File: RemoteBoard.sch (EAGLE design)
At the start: 10 parts, among them U1 SPG30, U2 TXS0102DCU, U3 MIC53651.8SC70, U4 BME280

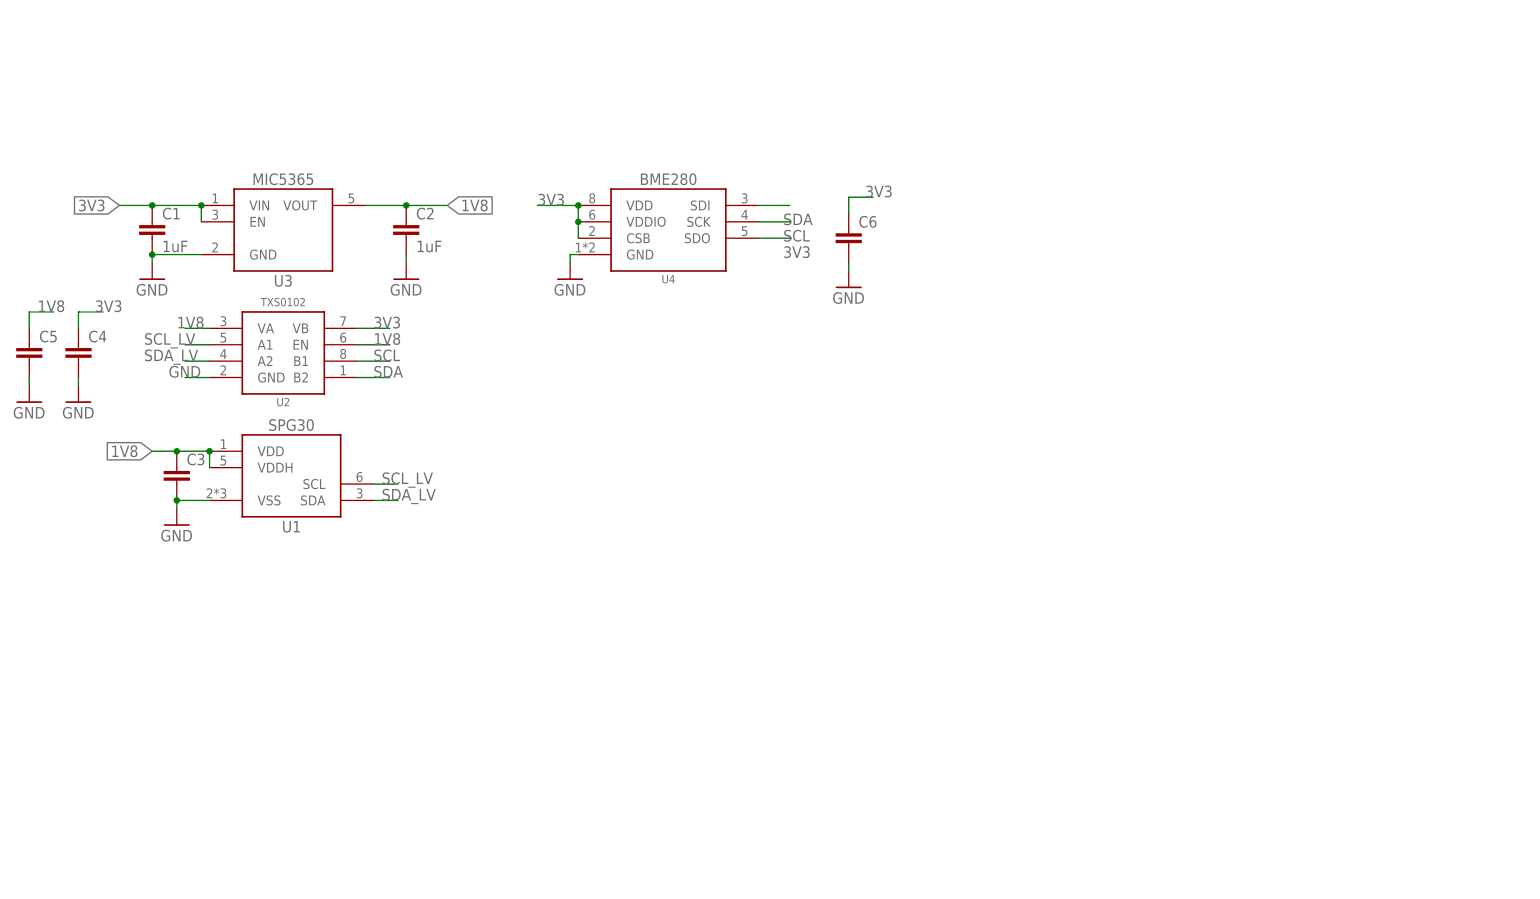
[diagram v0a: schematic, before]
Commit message: Continued schematic capture for remote board, layout begin
Schematic for remote board complete except for TCS3400, significant layout progress
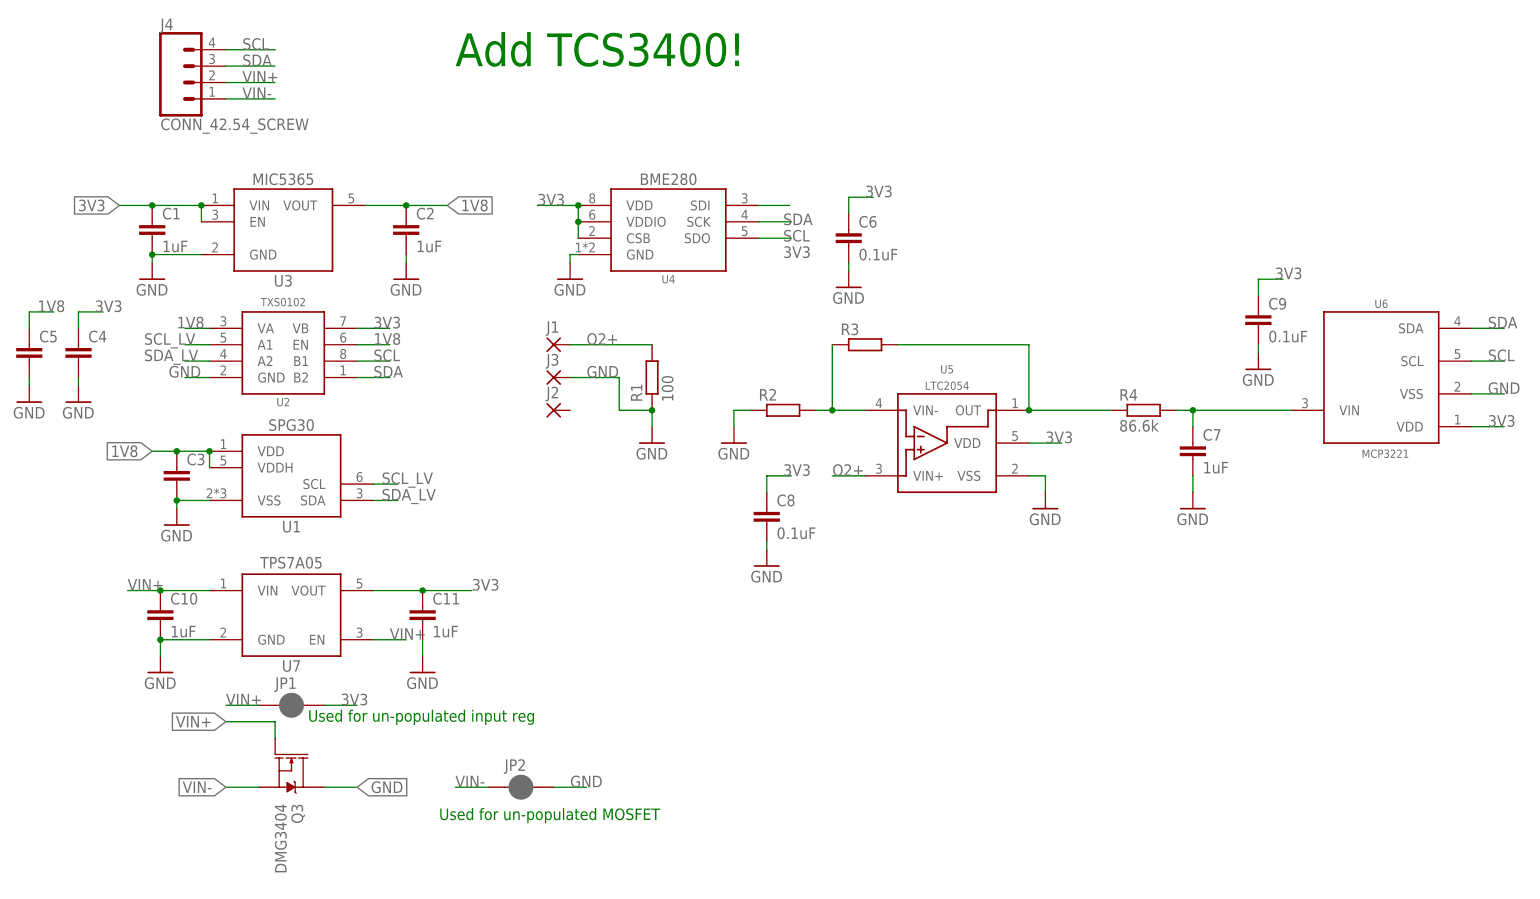
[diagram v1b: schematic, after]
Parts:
- added C10, C11: 1uF, bschulz_passives:C-EUC0805
- added C7: 1uF, bschulz:C-EUC0805
- added C8, C9: 0.1uF, bschulz:C-EUC0805
- added J1, J2, J3: SOCKETS9111, bschulz:SOCKETS9111
- added J4: CONN_42.54_SCREW, bschulz:CONN_42.54_SCREW
- added JP1, JP2: JUMPER-SMT_2_NC_PASTE_SILK, SparkFun-Jumpers:JUMPER-SMT_2_NC_PASTE_SILK
- added Q3: DMG3404, bschulz:MOSFET-NCH-DMG3404L
- added R1: 100, bschulz:R-EU_R0805
- added R2, R3: (no value), bschulz:R-EU_R0805
- added R4: 86.6k, bschulz:R-EU_R0805
- added U5: LTC2054, bschulz:LTC2054
- added U6: MCP3221, bschulz:MCP3221
- added U7: TPS7A0533DBV, bschulz:TPS7A0533DBV
- C1, C2: device bschulz_passives:C-EU1UFC0603 -> bschulz:C-EUC0805
- C3, C4, C5: device bschulz_passives:C-EU0.1UFC0603 -> bschulz:C-EUC0805
- C6: value (none) -> 0.1uF; device bschulz_passives:C-EU0.1UFC0603 -> bschulz:C-EUC0805
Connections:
- new net N$1: R2.2, R3.1, U5.VIN-
- new net N$2: R3.2, R4.1, U5.OUT
- new net N$3: C7.1, R4.2, U6.VIN
- new net O2+: J1.P, R1.2, U5.VIN+
- new net VIN+: C10.1, J4.2, JP1.1, Q3.G, U7.EN, U7.VIN
- new net VIN-: J4.1, JP2.1, Q3.S
- net 3V3: now also C11.1, C8.1, C9.1, JP1.2, U5.VDD, U6.VDD, U7.VOUT
- net GND: now also C10.2, C11.2, C7.2, C8.2, C9.2, J3.P, JP2.2, Q3.D, R1.1, R2.1, U5.VSS, U6.VSS, U7.GND
- net SCL: now also J4.4, U6.SCL
- net SDA: now also J4.3, U6.SDA
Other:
- note added: "Add TCS3400!"
- note added: "Used for un-populated MOSFET"
- note added: "Used for un-populated input reg"

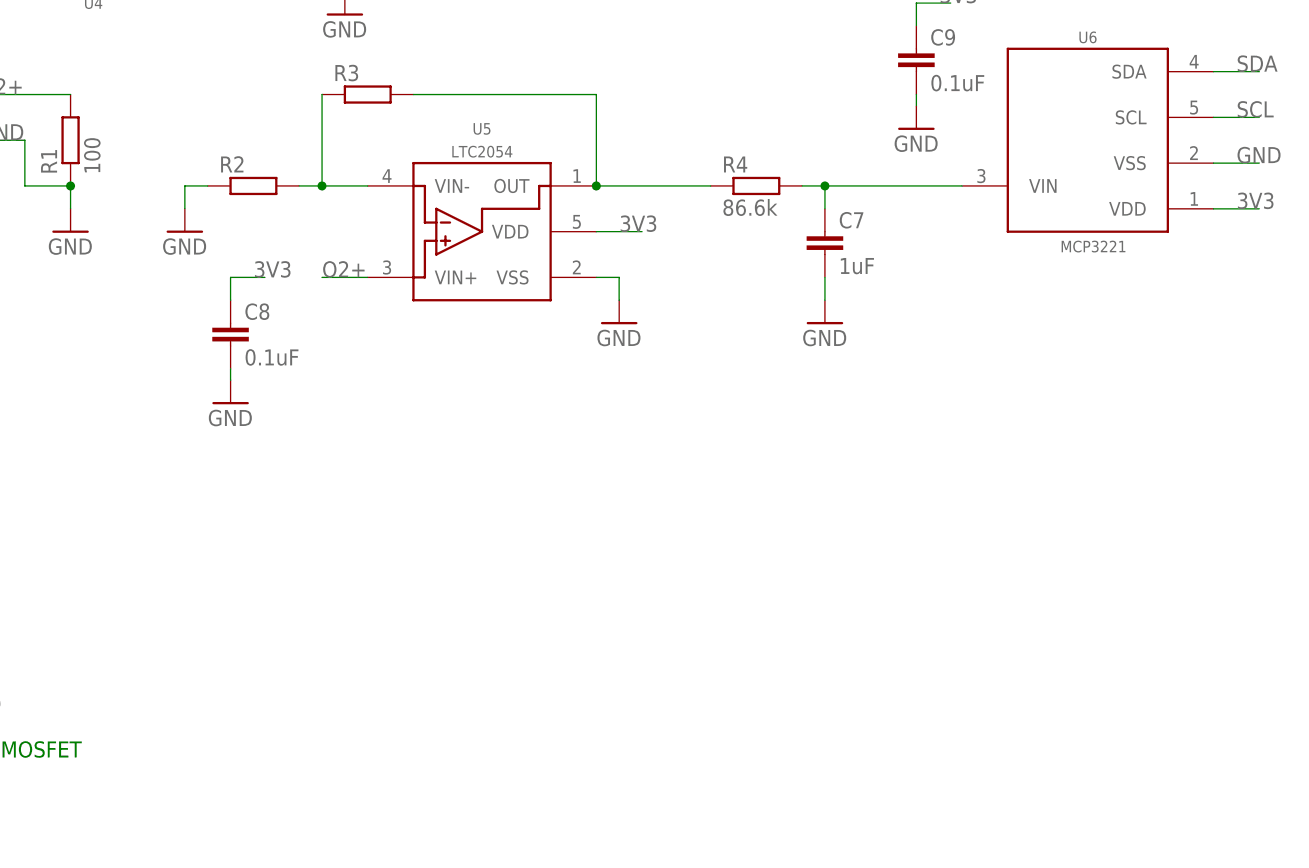
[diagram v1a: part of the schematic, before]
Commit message: Minor updates to Primary and Remote
Cleaned up/added silkscreen, added test points to both boards
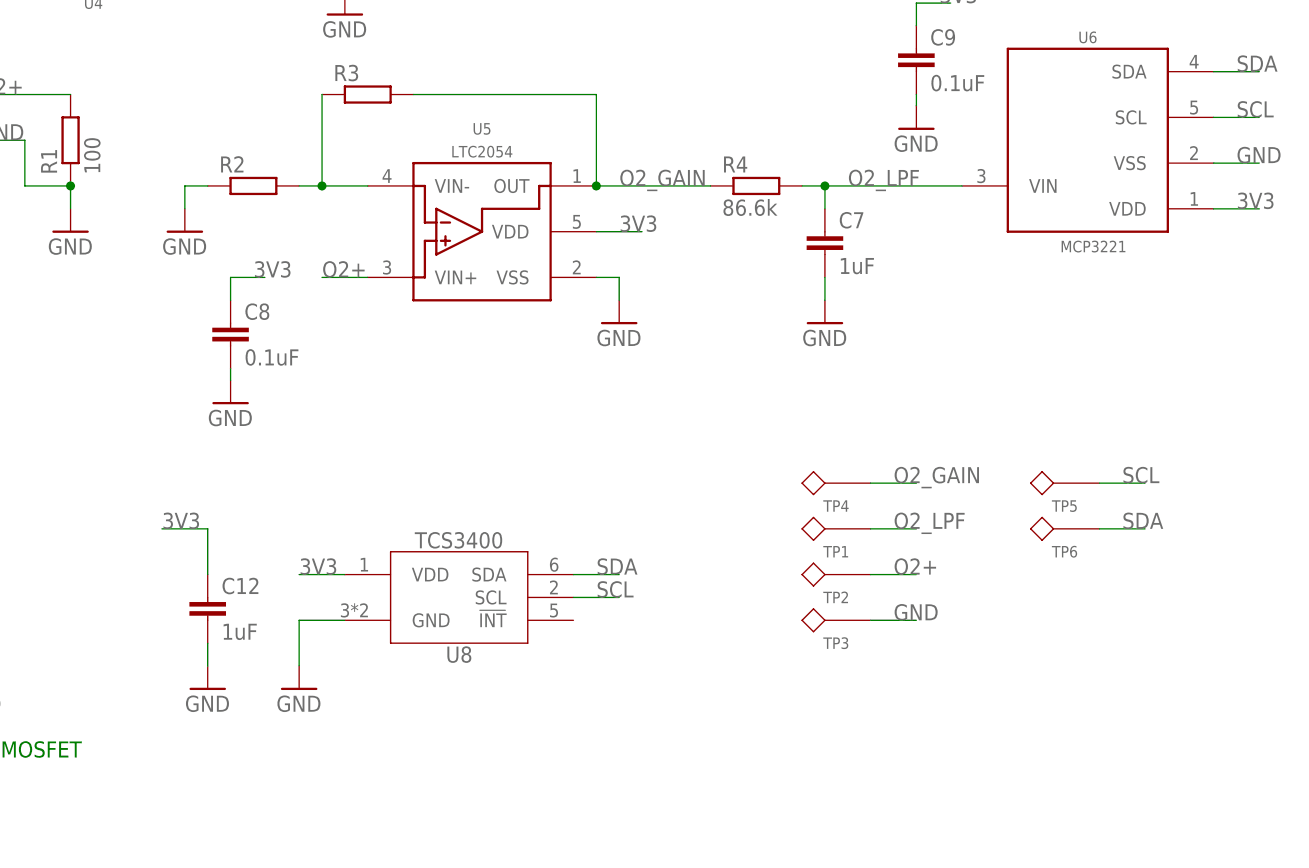
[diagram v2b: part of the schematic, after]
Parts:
- added C12: 1uF, bschulz_passives:C-EUC0805
- added TP1, TP2, TP3, TP4, TP5, TP6: TESTPOINTRCU, bschulz:TESTPOINTRCU
- added U8: TCS3400, bschulz:TCS3400
- C9: device bschulz:C-EUC0805 -> bschulz_passives:C-EUC0805
- J1, J2, J3: value SOCKETS9111 -> SOCKETS9111_SLOT; device bschulz:SOCKETS9111 -> bschulz:SOCKETS9111_SLOT
- R1, R2, R3, R4: device bschulz:R-EU_R0805 -> bschulz_passives:R-EU_R0805
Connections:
- removed net N$2: R3.2, R4.1, U5.OUT
- removed net N$3: C7.1, R4.2, U6.VIN
- new net O2_GAIN: R3.2, R4.1, TP4.P$1, U5.OUT
- new net O2_LPF: C7.1, R4.2, TP1.P$1, U6.VIN
- net 3V3: now also C12.1, U8.VDD
- net GND: now also C12.2, TP3.P$1, U8.GND
- net O2+: now also TP2.P$1
- net SCL: now also TP5.P$1, U8.SCL
- net SDA: now also TP6.P$1, U8.SDA
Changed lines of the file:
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@@
 <part name="C6" library="bschulz" deviceset="C-EU" device="C0805" value="0.1uF"/>
 <part name="GND7" library="supply1" library_urn="urn:adsk.eagle:library:371" deviceset="GND" device=""/>
-<part name="J1" library="bschulz" deviceset="SOCKET" device="S9111"/>
-<part name="J2" library="bschulz" deviceset="SOCKET" device="S9111"/>
-<part name="J3" library="bschulz" deviceset="SOCKET" device="S9111"/>
+<part name="J1" library="bschulz" deviceset="SOCKET" device="S9111_SLOT" value="SOCKETS9111_SLOT"/>
+<part name="J2" library="bschulz" deviceset="SOCKET" device="S9111_SLOT" value="SOCKETS9111_SLOT"/>
+<part name="J3" library="bschulz" deviceset="SOCKET" device="S9111_SLOT" value="SOCKETS9111_SLOT"/>
 <part name="U5" library="bschulz" deviceset="LTC2054" device=""/>
-<part name="R1" library="bschulz" deviceset="R-EU_" device="R0805" value="100"/>
+<part name="R1" library="bschulz_passives" deviceset="R-EU_" device="R0805" value="100"/>
 <part name="GND8" library="supply1" library_urn="urn:adsk.eagle:library:371" deviceset="GND" device=""/>
-<part name="R2" library="bschulz" deviceset="R-EU_" device="R0805"/>
-<part name="R3" library="bschulz" deviceset="R-EU_" device="R0805"/>
+<part name="R2" library="bschulz_passives" deviceset="R-EU_" device="R0805"/>
+<part name="R3" library="bschulz_passives" deviceset="R-EU_" device="R0805"/>
 <part name="GND9" library="supply1" library_urn="urn:adsk.eagle:library:371" deviceset="GND" device=""/>
 <part name="GND10" library="supply1" library_urn="urn:adsk.eagle:library:371" deviceset="GND" device=""/>
-<part name="R4" library="bschulz" deviceset="R-EU_" device="R0805" value="86.6k"/>
+<part name="R4" library="bschulz_passives" deviceset="R-EU_" device="R0805" value="86.6k"/>
 <part name="C7" library="bschulz" deviceset="C-EU" device="C0805" value="1uF"/>
 <part name="GND11" library="supply1" library_urn="urn:adsk.eagle:library:371" deviceset="GND" device=""/>
@@
 <part name="GND12" library="supply1" library_urn="urn:adsk.eagle:library:371" deviceset="GND" device=""/>
 <part name="J4" library="bschulz" deviceset="CONN_4" device="2.54_SCREW"/>
-<part name="C9" library="bschulz" deviceset="C-EU" device="C0805" value="0.1uF"/>
+<part name="C9" library="bschulz_passives" deviceset="C-EU" device="C0805" value="0.1uF"/>
 <part name="GND13" library="supply1" library_urn="urn:adsk.eagle:library:371" deviceset="GND" device=""/>
 <part name="U7" library="bschulz" deviceset="TPS7A05*" device="DBV" technology="33"/>
@@
 <part name="JP1" library="SparkFun-Jumpers" library_urn="urn:adsk.eagle:library:528" deviceset="JUMPER-SMT_2_NC_PASTE" device="_SILK" package3d_urn="urn:adsk.eagle:package:39282/1"/>
 <part name="JP2" library="SparkFun-Jumpers" library_urn="urn:adsk.eagle:library:528" deviceset="JUMPER-SMT_2_NC_PASTE" device="_SILK" package3d_urn="urn:adsk.eagle:package:39282/1"/>
+<part name="U8" library="bschulz" deviceset="TCS3400" device=""/>
+<part name="GND16" library="supply1" library_urn="urn:adsk.eagle:library:371" deviceset="GND" device=""/>
+<part name="C12" library="bschulz_passives" deviceset="C-EU" device="C0805" value="1uF"/>
+<part name="GND17" library="supply1" library_urn="urn:adsk.eagle:library:371" deviceset="GND" device=""/>
+<part name="TP1" library="bschulz" deviceset="TESTPOINT" device="RCU"/>
+<part name="TP2" library="bschulz" deviceset="TESTPOINT" device="RCU"/>
+<part name="TP3" library="bschulz" deviceset="TESTPOINT" device="RCU"/>
+<part name="TP4" library="bschulz" deviceset="TESTPOINT" device="RCU"/>
+<part name="TP5" library="bschulz" deviceset="TESTPOINT" device="RCU"/>
+<part name="TP6" library="bschulz" deviceset="TESTPOINT" device="RCU"/>
 </parts>
 <sheets>
@@
 <attribute name="NAME" x="78.74" y="-20.32" size="1.778" layer="95" font="vector"/>
 </instance>
+<instance part="U8" gate="G$1" x="144.78" y="-10.16" smashed="yes">
+<attribute name="NAME" x="144.78" y="-16.51" size="1.778" layer="95" ratio="15" align="center"/>
+</instance>
+<instance part="GND16" gate="1" x="127" y="-20.32" smashed="yes">
+<attribute name="VALUE" x="124.46" y="-22.86" size="1.778" layer="96"/>
+</instance>
+<instance part="C12" gate="G$1" x="116.84" y="-10.16" smashed="yes">
+<attribute name="NAME" x="118.364" y="-9.779" size="1.778" layer="95"/>
+<attribute name="VALUE" x="118.364" y="-14.859" size="1.778" layer="96"/>
+</instance>
+<instance part="GND17" gate="1" x="116.84" y="-20.32" smashed="yes">
+<attribute name="VALUE" x="114.3" y="-22.86" size="1.778" layer="96"/>
+</instance>
+<instance part="TP1" gate="G$1" x="190.5" y="-2.54" smashed="yes" rot="R90">
+<attribute name="NAME" x="186.69" y="-5.08" size="1.27" layer="95" rot="R180" align="center"/>
+</instance>
+<instance part="TP2" gate="G$1" x="190.5" y="-7.62" smashed="yes" rot="R90">
+<attribute name="NAME" x="186.69" y="-10.16" size="1.27" layer="95" rot="R180" align="center"/>
+</instance>
+<instance part="TP3" gate="G$1" x="190.5" y="-12.7" smashed="yes" rot="R90">
+<attribute name="NAME" x="186.69" y="-15.24" size="1.27" layer="95" rot="R180" align="center"/>
+</instance>
+<instance part="TP4" gate="G$1" x="190.5" y="2.54" smashed="yes" rot="R90">
+<attribute name="NAME" x="186.69" y="0" size="1.27" layer="95" rot="R180" align="center"/>
+</instance>
+<instance part="TP5" gate="G$1" x="215.9" y="2.54" smashed="yes" rot="R90">
+<attribute name="NAME" x="212.09" y="0" size="1.27" layer="95" rot="R180" align="center"/>
+</instance>
+<instance part="TP6" gate="G$1" x="215.9" y="-2.54" smashed="yes" rot="R90">
+<attribute name="NAME" x="212.09" y="-5.08" size="1.27" layer="95" rot="R180" align="center"/>
+</instance>
 </instances>
 <busses>
@@
 <label x="162.56" y="30.48" size="1.778" layer="95"/>
 </segment>
+<segment>
+<pinref part="U8" gate="G$1" pin="VDD"/>
+<wire x1="132.08" y1="-7.62" x2="127" y2="-7.62" width="0.1524" layer="91"/>
+<label x="127" y="-7.62" size="1.778" layer="95"/>
+</segment>
+<segment>
+<pinref part="C12" gate="G$1" pin="1"/>
+<wire x1="116.84" y1="-7.62" x2="116.84" y2="-2.54" width="0.1524" layer="91"/>
+<wire x1="116.84" y1="-2.54" x2="111.76" y2="-2.54" width="0.1524" layer="91"/>
+<label x="111.76" y="-2.54" size="1.778" layer="95"/>
+</segment>
 </net>
 <net name="GND" class="0">
@@
 <label x="88.9" y="-22.86" size="1.778" layer="95"/>
 </segment>
+<segment>
+<pinref part="U8" gate="G$1" pin="GND"/>
+<wire x1="132.08" y1="-12.7" x2="127" y2="-12.7" width="0.1524" layer="91"/>
+<wire x1="127" y1="-12.7" x2="127" y2="-17.78" width="0.1524" layer="91"/>
+<pinref part="GND16" gate="1" pin="GND"/>
+</segment>
+<segment>
+<pinref part="GND17" gate="1" pin="GND"/>
+<pinref part="C12" gate="G$1" pin="2"/>
+<wire x1="116.84" y1="-17.78" x2="116.84" y2="-15.24" width="0.1524" layer="91"/>
+</segment>
+<segment>
+<pinref part="TP3" gate="G$1" pin="P$1"/>
+<wire x1="190.5" y1="-12.7" x2="195.58" y2="-12.7" width="0.1524" layer="91"/>
+<label x="193.04" y="-12.7" size="1.778" layer="95"/>
+</segment>
 </net>
 <net name="1V8" class="0">
@@
 <label x="38.1" y="88.9" size="1.778" layer="95"/>
 </segment>
+<segment>
+<pinref part="U8" gate="G$1" pin="SDA"/>
+<wire x1="157.48" y1="-7.62" x2="162.56" y2="-7.62" width="0.1524" layer="91"/>
+<label x="160.02" y="-7.62" size="1.778" layer="95"/>
+</segment>
+<segment>
+<pinref part="TP6" gate="G$1" pin="P$1"/>
+<wire x1="215.9" y1="-2.54" x2="220.98" y2="-2.54" width="0.1524" layer="91"/>
+<label x="218.44" y="-2.54" size="1.778" layer="95"/>
+</segment>
 </net>
 <net name="SCL" class="0">
@@
 <wire x1="35.56" y1="91.44" x2="43.18" y2="91.44" width="0.1524" layer="91"/>
 <label x="38.1" y="91.44" size="1.778" layer="95"/>
+</segment>
+<segment>
+<pinref part="U8" gate="G$1" pin="SCL"/>
+<wire x1="157.48" y1="-10.16" x2="162.56" y2="-10.16" width="0.1524" layer="91"/>
+<label x="160.02" y="-10.16" size="1.778" layer="95"/>
+</segment>
+<segment>
+<pinref part="TP5" gate="G$1" pin="P$1"/>
+<wire x1="215.9" y1="2.54" x2="220.98" y2="2.54" width="0.1524" layer="91"/>
+<label x="218.44" y="2.54" size="1.778" layer="95"/>
 </segment>
 </net>
@@
 <wire x1="134.62" y1="25.4" x2="129.54" y2="25.4" width="0.1524" layer="91"/>
 <label x="129.54" y="25.4" size="1.778" layer="95"/>
+</segment>
+<segment>
+<pinref part="TP2" gate="G$1" pin="P$1"/>
+<wire x1="190.5" y1="-7.62" x2="195.58" y2="-7.62" width="0.1524" layer="91"/>
+<label x="193.04" y="-7.62" size="1.778" layer="95"/>
 </segment>
 </net>
@@
 </segment>
 </net>
-<net name="N$2" class="0">
+<net name="O2_GAIN" class="0">
 <segment>
 <pinref part="R3" gate="G$1" pin="2"/>
@@
 <junction x="160.02" y="35.56"/>
 <pinref part="R4" gate="G$1" pin="1"/>
-</segment>
-</net>
-<net name="N$3" class="0">
+<label x="162.56" y="35.56" size="1.778" layer="95"/>
+</segment>
+<segment>
+<pinref part="TP4" gate="G$1" pin="P$1"/>
+<wire x1="190.5" y1="2.54" x2="195.58" y2="2.54" width="0.1524" layer="91"/>
+<label x="193.04" y="2.54" size="1.778" layer="95"/>
+</segment>
+</net>
+<net name="O2_LPF" class="0">
 <segment>
 <pinref part="R4" gate="G$1" pin="2"/>
@@
 <pinref part="U6" gate="G$1" pin="VIN"/>
 <wire x1="200.66" y1="35.56" x2="185.42" y2="35.56" width="0.1524" layer="91"/>
-</segment>
-</net>
+<label x="187.96" y="35.56" size="1.778" layer="95"/>
+</segment>
+<segment>
+<pinref part="TP1" gate="G$1" pin="P$1"/>
+<wire x1="190.5" y1="-2.54" x2="195.58" y2="-2.54" width="0.1524" layer="91"/>
+<label x="193.04" y="-2.54" size="1.778" layer="95"/>
+</segment>
+</net>

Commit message: Minor cleanup/fixes to boards, generated gerbers
Minor changes to boards, primarily cleanup and generated gerbers for fab, ready for review
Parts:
- R2: value (none) -> 1k
- R3: value (none) -> 78.7k
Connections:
- net 1V8: now also C12.1, U8.VDD
- net 3V3: no longer C12.1, U8.VDD
- net GND: now also J1.P, R1.2; no longer J3.P, R1.1
- net O2+: now also J3.P, R1.1; no longer J1.P, R1.2
- net SCL: no longer U8.SCL
- net SCL_LV: now also U8.SCL
- net SDA: no longer U8.SDA
- net SDA_LV: now also U8.SDA
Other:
- note added: "ADR = 0x39"
- note added: "ADR = 0x4D"
- note added: "ADR = 0x58"
- note added: "ADR = 0x77"
- note removed: "Add TCS3400!"
